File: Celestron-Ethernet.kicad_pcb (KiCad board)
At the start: 4 copper layers, 90.4 x 33.3 mm, 59 parts, among them J2 6P6C, J3 RJ45_Abracon_ARJP11A-MASA-B-A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, U2 LP2985-5.0, U3 LP2985-3.3

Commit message: Initial routing
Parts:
- added REF**: MountingHole_3.2mm_M3, MountingHole:MountingHole_3.2mm_M3, F.Cu at (189.7, 97.5)
- added REF**: MountingHole_3.2mm_M3, MountingHole:MountingHole_3.2mm_M3, F.Cu at (108.2, 97.5)
- added REF**: MountingHole_3.2mm_M3, MountingHole:MountingHole_3.2mm_M3, F.Cu at (108.2, 72.9)
- moved R15 4.57 mm to (133.6, 97.3)
- moved C17 4.57 mm to (124.5, 97.3), turned to 270 degrees
- moved C13 2.29 mm to (131.3, 97.3)
- moved C14 2.29 mm to (129.0, 97.3)
- moved R25 2.29 mm to (119.9, 97.3), turned to 270 degrees
- moved C15 2.29 mm to (122.2, 97.3)
- moved W5500 1.02 mm to (134.1, 85.2)
- moved DHCP 0.92 mm to (187.2, 74.9)
- moved C3 0.92 mm to (160.3, 76.7)
- moved R1 0.92 mm to (162.6, 76.7)
- moved R2 0.92 mm to (164.8, 76.7)
- moved USB 0.77 mm to (162.6, 72.1)
- moved USB PWR 0.76 mm to (170.9, 73.7)
- moved 25Mhz 0.51 mm to (143.0, 85.2)
- moved U2 0.25 mm to (173.0, 97.3)
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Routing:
- net GND: track 0.00 -> 78.3 mm, vias 0 -> 4
- net Net-(C5-Pad1): track 0.00 -> 56.4 mm, vias 0 -> 2
- net Net-(C17-Pad1): track 0.00 -> 29.6 mm
- net Net-(SW1-Pad2): track 0.00 -> 19.8 mm
- net Net-(J2-Pad2): track 0.00 -> 19.1 mm
- net Net-(J2-Pad6): track 0.00 -> 15.4 mm
- net Net-(R16-Pad2): track 0.00 -> 14.4 mm
- net Net-(J1-Pad6): track 0.00 -> 12.6 mm
- net Net-(C18-Pad2): track 0.00 -> 12.3 mm
- net Net-(R12-Pad2): track 0.00 -> 11.6 mm
- net Net-(R18-Pad2): track 0.00 -> 11.2 mm
- net Net-(J3-Pad2): track 0.00 -> 11.1 mm
- net Net-(R14-Pad2): track 0.00 -> 11.0 mm
- net Net-(D3-Pad1): track 0.00 -> 10.8 mm
- net Net-(C7-Pad2): track 0.00 -> 10.3 mm
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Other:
- board size 90.4 x 33.3 mm -> 88.9 x 31.8 mm
- net class Default: clearance 0.2 -> 0.1524; trace_width 0.25 -> 0.1524; via_dia 0.8 -> 0.4572; via_drill 0.4 -> 0.2286
- net class Power added: clearance 0.1524, trace_width 0.4064, via_dia 0.8128, via_drill 0.4064
- rule pad_to_mask_clearance: 0 -> 0.0508
- rule trace_clearance: 0.2 -> 0.1524
- rule trace_min: 0.2 -> 0.1524
- rule via_min_drill: 0.3 -> 0.2286
- rule via_min_size: 0.4 -> 0.4572

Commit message: bypass caps
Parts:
- removed the REF** at (108.2, 72.9)
- added C19: 6.8nF, Capacitor_SMD:C_0603_1608Metric, F.Cu at (114.8, 110.5)
- added C20: 100nF, Capacitor_SMD:C_0603_1608Metric, F.Cu at (126.2, 98.6)
- added C21: 100nF, Capacitor_SMD:C_0603_1608Metric, F.Cu at (126.2, 94.7)
- added C22: 6.8nF, Capacitor_SMD:C_0603_1608Metric, F.Cu at (124.0, 110.5)
- added C23: 22nF, Capacitor_SMD:C_0603_1608Metric, F.Cu at (117.1, 86.6)
- added C24: 100nF, Capacitor_SMD:C_0603_1608Metric, F.Cu at (130.8, 106.2)
- added C25: 100nF, Capacitor_SMD:C_0603_1608Metric, F.Cu at (135.4, 106.2)
- added C26: 100nF, Capacitor_SMD:C_0603_1608Metric, F.Cu at (133.1, 106.2)
- added C27: 1nF/2KV, Capacitor_SMD:C_0603_1608Metric, F.Cu at (112.5, 110.5)
- added FB1: HH-1M1608-121JT, Inductor_SMD:L_0603_1608Metric, F.Cu at (137.7, 106.2)
- added REF**: MountingHole_3.2mm_M3, MountingHole:MountingHole_3.2mm_M3, F.Cu at (186.9, 86.1)
- added REF**: MountingHole_3.2mm_M3, MountingHole:MountingHole_3.2mm_M3, F.Cu at (105.2, 86.1)
- C15: value 10nF -> 10uF
- C16: value 6.8nF -> 100nF
- C17: value 6.8nF -> 10nF
- C18: value 22nF -> 100nF
- JP1: renamed from USB PWR
- R18: value 12K4 -> 12.4K
- moved C18 29.6 mm to (126.2, 102.4)
- moved R22 26.0 mm to (135.4, 110.5)
- moved C16 25.2 mm to (140.0, 102.4)
- moved C15 20.7 mm to (142.2, 102.4), turned to 270 degrees
- moved SW1 16.5 mm to (177.3, 88.1)
- moved C3 16.4 mm to (150.6, 89.9)
- moved R1 16.2 mm to (153.2, 89.9)
- moved R2 16.1 mm to (155.7, 89.9)
- moved J1 15.6 mm to (154.2, 85.3)
- moved JP1 15.6 mm to (162.6, 86.9)
- moved R3 15.5 mm to (150.6, 102.4)
- moved REF** 13.6 mm to (105.2, 110.7)
- moved D3 13.5 mm to (169.7, 98.4)
- moved U1 13.5 mm to (159.9, 98.4)
- moved C1 13.5 mm to (162.1, 112.3)
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- renumbered C8 to C10, C10 to C11, C11 to C5, C9 to C6, C5 to C7, C6 to C8, C7 to C9, PWR to D4, USB to J1, DHCP to SW1, ATmega32U4-AU to U1, W5500 to U4, 16MHz to Y1, 25Mhz to Y2
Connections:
- net Net-(C5-Pad1) renamed /12V
- C15 pad 1: GND -> +3V3
- C15 pad 2: Net-(C15-Pad2) -> GND
- C16 pad 1: Net-(C16-Pad1) -> +3V3
- C16 pad 2: Net-(C16-Pad2) -> GND
- C17 pad 1: Net-(C17-Pad1) -> GND
- C18 pad 1: GND -> +3.3VA
- C18 pad 2: Net-(C18-Pad2) -> GND
- J3 pad 15: Net-(J3-Pad15) -> GNDPWR
- J3 pad 3: Net-(C17-Pad1) -> Net-(C22-Pad1)
- J3 pad 4: Net-(C18-Pad2) -> Net-(C23-Pad2)
- J3 pad 5: Net-(C15-Pad2) -> Net-(C17-Pad2)
- J3 pad 6: Net-(C16-Pad1) -> Net-(C19-Pad1)
- R24 pad 1: Net-(C15-Pad2) -> Net-(C17-Pad2)
- R24 pad 2: Net-(C16-Pad2) -> Net-(C19-Pad2)
- R25 pad 1: Net-(C15-Pad2) -> Net-(C17-Pad2)
- R25 pad 2: Net-(C17-Pad2) -> Net-(C22-Pad2)
- R26 pad 1: Net-(C18-Pad2) -> Net-(C23-Pad2)
- U4 pad 11: +3V3 -> +3.3VA
- U4 pad 15: +3V3 -> +3.3VA
- U4 pad 17: +3V3 -> +3.3VA
- U4 pad 21: +3V3 -> +3.3VA
- U4 pad 4: +3V3 -> +3.3VA
- U4 pad 5: Net-(C16-Pad1) -> Net-(C19-Pad1)
- U4 pad 6: Net-(C17-Pad1) -> Net-(C22-Pad1)
- U4 pad 8: +3V3 -> +3.3VA
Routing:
- net GND: track 78.3 -> 0.00 mm, vias 4 -> 0
- net /12V: track 56.4 -> 0.00 mm, vias 2 -> 0
- net Net-(C17-Pad1): track 29.6 -> 0.00 mm
- net Net-(SW1-Pad2): track 19.8 -> 0.00 mm
- net Net-(J2-Pad2): track 19.1 -> 0.00 mm
- net Net-(J2-Pad6): track 15.4 -> 0.00 mm
- net Net-(R16-Pad2): track 14.4 -> 0.00 mm
- net Net-(J1-Pad6): track 12.6 -> 0.00 mm
- net Net-(C18-Pad2): track 12.3 -> 0.00 mm
- net Net-(R12-Pad2): track 11.6 -> 0.00 mm
- net Net-(R18-Pad2): track 11.2 -> 0.00 mm
- net Net-(J3-Pad2): track 11.1 -> 0.00 mm
- net Net-(R14-Pad2): track 11.0 -> 0.00 mm
- net Net-(D3-Pad1): track 10.8 -> 0.00 mm
- net Net-(C9-Pad2): track 10.3 -> 0.00 mm
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
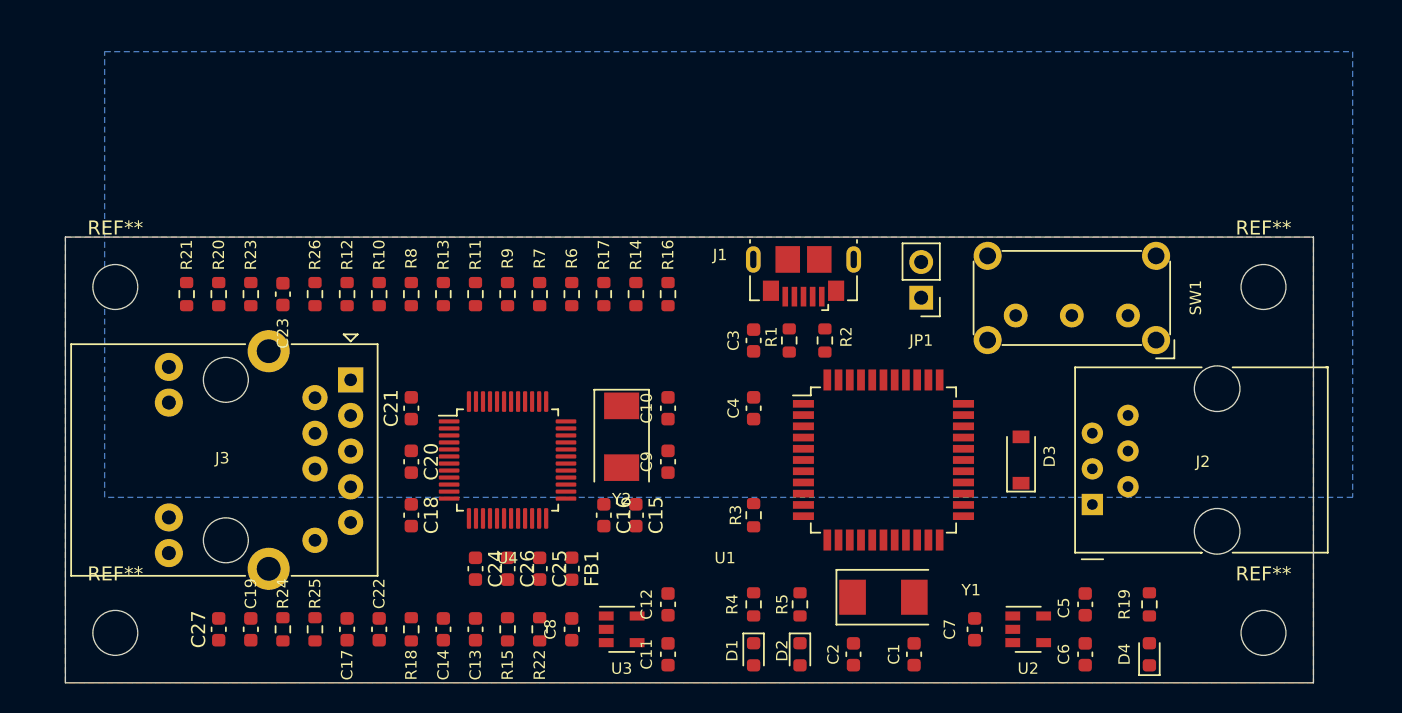
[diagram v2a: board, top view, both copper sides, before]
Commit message: corrected w5500 schematic, added mounting holes
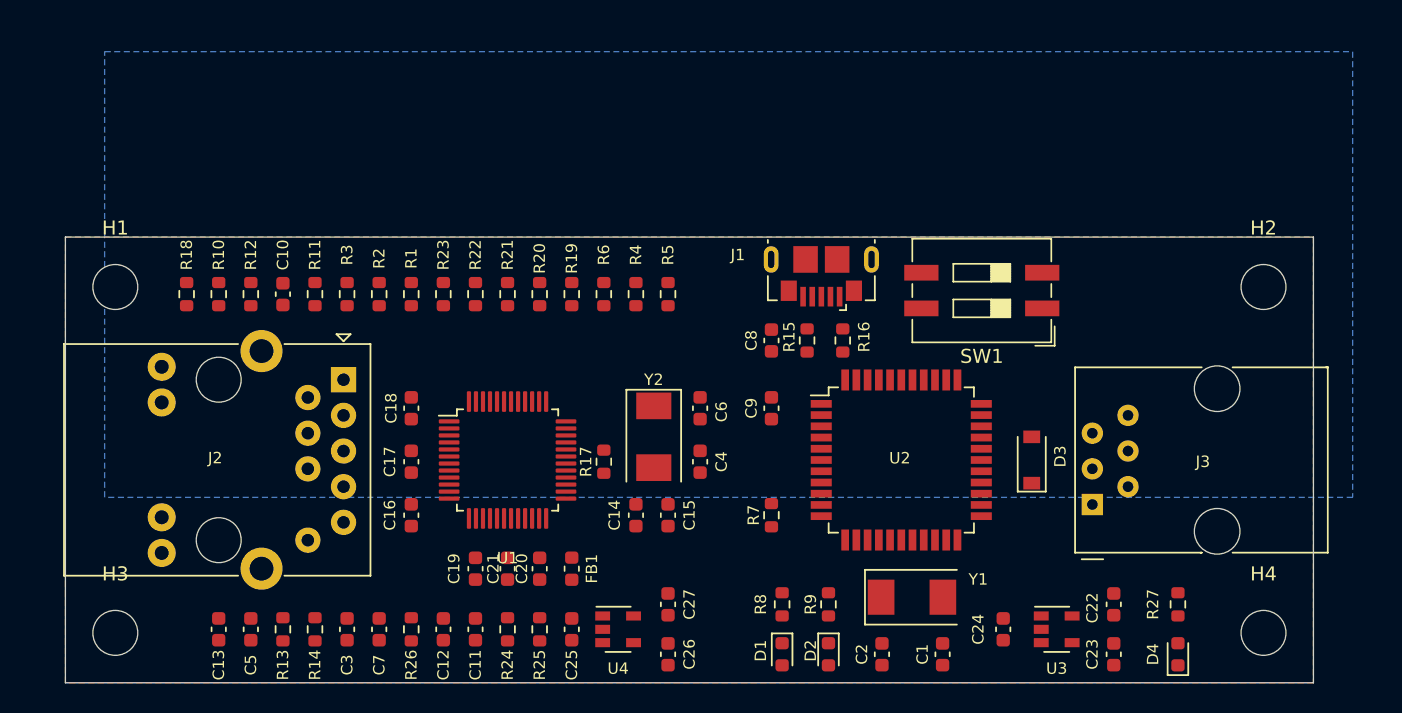
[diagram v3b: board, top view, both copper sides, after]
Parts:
- removed the C3 at (150.6, 89.9)
- removed the C4 at (150.6, 94.7)
- removed JP1: USB PWR, Connector_PinHeader_2.54mm:PinHeader_1x02_P2.54mm_Vertical
- removed the R3 at (150.6, 102.4)
- removed REF** (x4): MountingHole_3.2mm_M3, MountingHole:MountingHole_3.2mm_M3
- removed the U1 at (159.9, 98.4)
- added C8: 100nF, Capacitor_SMD:C_0603_1608Metric, F.Cu at (151.9, 89.9)
- added C9: 100nF, Capacitor_SMD:C_0603_1608Metric, F.Cu at (151.9, 94.7)
- added H1: MountingHole, MountingHole:MountingHole_3.2mm_M3, F.Cu at (105.2, 86.1)
- added H2: MountingHole, MountingHole:MountingHole_3.2mm_M3, F.Cu at (186.9, 86.1)
- added H3: MountingHole, MountingHole:MountingHole_3.2mm_M3, F.Cu at (105.2, 110.7)
- added H4: MountingHole, MountingHole:MountingHole_3.2mm_M3, F.Cu at (186.9, 110.7)
- added R17: 1M, Resistor_SMD:R_0603_1608Metric, F.Cu at (140.0, 98.6)
- added R7: 10K, Resistor_SMD:R_0603_1608Metric, F.Cu at (151.9, 102.4)
- added U2: ATmega32U4-AU, Package_QFP:TQFP-44_10x10mm_P0.8mm, F.Cu at (161.1, 98.4)
- FB1: value HH-1M1608-121JT -> 60 ohm/100MHz
- SW1: value SW_SPDT -> SW_DIP_x02; footprint Button_Switch_THT:SW_E-Switch_EG1224_SPDT_Angled -> Button_Switch_SMD:SW_DIP_SPSTx02_Slide_9.78x7.26mm_W8.61mm_P2.54mm
- moved SW1 10.6 mm to (166.9, 86.4)
- moved C14 2.29 mm to (144.5, 102.4)
- moved C15 2.29 mm to (142.2, 102.4)
- moved C4 2.29 mm to (146.8, 98.6)
- moved C6 2.29 mm to (146.8, 94.7)
- moved Y2 2.29 mm to (143.5, 96.8)
- moved C1 2.03 mm to (164.1, 112.3)
- moved C22 2.03 mm to (176.3, 108.7)
- moved C23 2.03 mm to (176.3, 112.3)
- moved D4 2.03 mm to (180.8, 112.3)
- moved R27 2.03 mm to (180.8, 108.7)
- moved Y1 2.03 mm to (161.9, 108.2)
- moved C2 2.03 mm to (159.8, 112.3)
- moved C24 2.03 mm to (168.4, 110.5)
- moved D1 2.03 mm to (152.7, 112.3)
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- renumbered C23 to C10, C13 to C11, C14 to C12, C27 to C13, C15 to C14, C16 to C15, C18 to C16, C20 to C17, C21 to C18, C24 to C19, C25 to C20, C26 to C21, C5 to C22, C6 to C23, C7 to C24, C8 to C25, C11 to C26, C12 to C27, C17 to C3, C9 to C4, C19 to C5, C10 to C6, C22 to C7, J3 to J2, J2 to J3, R8 to R1, R20 to R10, R26 to R11, R23 to R12, R24 to R13, R25 to R14, R1 to R15, R2 to R16, R21 to R18, R6 to R19, R10 to R2, R7 to R20, R9 to R21, R11 to R22, R13 to R23, R15 to R24, R22 to R25, R18 to R26, R19 to R27, R12 to R3, R14 to R4, R16 to R5, R17 to R6, R4 to R8, R5 to R9, U4 to U1, U2 to U3, U3 to U4
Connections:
- C5 pad 1: Net-(C19-Pad1) -> Net-(C5-Pad1)
- C5 pad 2: Net-(C19-Pad2) -> Net-(C5-Pad2)
- C7 pad 1: Net-(C22-Pad1) -> Net-(C7-Pad1)
- C7 pad 2: Net-(C22-Pad2) -> Net-(C7-Pad2)
- J1 pad 1: Net-(J1-Pad1) -> /USB_PWR
- J2 pad 3: Net-(C22-Pad1) -> Net-(C7-Pad1)
- J2 pad 6: Net-(C19-Pad1) -> Net-(C5-Pad2)
- R13 pad 2: Net-(C19-Pad2) -> Net-(C5-Pad1)
- R14 pad 2: Net-(C22-Pad2) -> Net-(C7-Pad2)
- R4 pad 2: Net-(R14-Pad2) -> Net-(R4-Pad2)
- R5 pad 2: Net-(R16-Pad2) (its old number) -> Net-(R5-Pad2)
- R6 pad 1: Net-(R17-Pad1) -> +3V3
- R6 pad 2: GND -> Net-(R6-Pad2)
- SW1 pad 1: GND -> /USB_PWR
- SW1 pad 2: Net-(SW1-Pad2) -> /DCHP_ENA
- SW1 pad 3: Net-(SW1-Pad3) -> GND
- U1 pad 32: Net-(R16-Pad2) (its old number) -> Net-(R6-Pad2)
- U1 pad 36: Net-(R14-Pad2) -> Net-(R5-Pad2)
- U1 pad 37: Net-(R17-Pad1) -> Net-(R4-Pad2)
- U1 pad 5: Net-(C19-Pad1) -> Net-(C5-Pad1)
- U1 pad 6: Net-(C22-Pad1) -> Net-(C7-Pad2)

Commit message: traces complete
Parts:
- removed the C15 at (142.2, 102.4)
- removed the C25 at (137.7, 110.5)
- removed the C4 at (146.8, 98.6)
- removed the C9 at (151.9, 94.7)
- removed D4: Red, LED_SMD:LED_0603_1608Metric
- removed the R14 at (119.4, 110.5)
- removed the R15 at (154.4, 89.9)
- removed R25: 330R, Resistor_SMD:R_0603_1608Metric
- removed R26: 12.4K, Resistor_SMD:R_0603_1608Metric
- removed R27: 1K, Resistor_SMD:R_0603_1608Metric
- removed the R8 at (152.7, 108.7)
- removed the R9 at (156.0, 108.7)
- removed the U4 at (141.0, 110.5)
- added C1: 100nF, Capacitor_SMD:C_0603_1608Metric, F.Cu at (171.4, 94.5)
- added C10: 100nF, Capacitor_SMD:C_0603_1608Metric, F.Cu at (167.4, 90.7)
- added C20: 100nF, Capacitor_SMD:C_0603_1608Metric, F.Cu at (138.9, 102.4)
- added C22: 100nF, Capacitor_SMD:C_0603_1608Metric, F.Cu at (171.4, 98.6)
- added C23: 100nF, Capacitor_SMD:C_0603_1608Metric, F.Cu at (157.2, 94.5)
- added C27: 1uF, Capacitor_SMD:C_0603_1608Metric, F.Cu at (141.0, 110.2)
- added C28: 1uF, Capacitor_SMD:C_0603_1608Metric, F.Cu at (153.2, 110.2)
- added R10: 330R, Resistor_SMD:R_0603_1608Metric, F.Cu at (171.4, 102.4)
- added R11: 82R, Resistor_SMD:R_0603_1608Metric, F.Cu at (124.7, 110.2)
- added R12: 82R, Resistor_SMD:R_0603_1608Metric, F.Cu at (126.7, 110.2)
- added R23: 12.4K, Resistor_SMD:R_0603_1608Metric, F.Cu at (132.8, 110.2)
- added SW2: DHCP, Button_Switch_THT:SW_E-Switch_EG1224_SPDT_Angled, F.Cu at (168.9, 108.7)
- added U3: LP2985-3.3, Package_TO_SOT_SMD:SOT-23-5, F.Cu at (144.0, 110.2)
- C11: value 10nF -> 1nF/2KV; footprint Capacitor_SMD:C_0603_1608Metric -> Capacitor_SMD:C_1206_3216Metric
- C13: value 1nF/2KV -> 10nF
- C2: renamed from C1; value 22pF -> 18pF
- C24: value 1uF -> 10uF
- C3: value 10nF -> 6.8nF
- C4: renamed from C2; value 22pF -> 18pF
- C7: value 6.8nF -> 18pF
- C8: value 100nF -> 10nF
- D1: value Ylw -> Red
- D2: value Grn -> 1N4148W; footprint LED_SMD:LED_0603_1608Metric -> Diode_SMD:D_SOD-323F
- D3: value 1N4148W -> Red; footprint Diode_SMD:D_SOD-123 -> LED_SMD:LED_0603_1608Metric
- J1: value USB_B_Micro -> FTDI; footprint Connector_USB:USB_Micro-B_GCT_USB3076-30-A -> Connector_PinHeader_2.54mm:PinHeader_1x06_P2.54mm_Horizontal
- J2: value RJ45_Abracon_ARJP11A-MASA-B-A-EMU2 -> RJ45_Amphenol_RJMG1BD3B8K1ANR; footprint Connector_RJ:RJ45_Abracon_ARJP11A-MA_Horizontal -> Connector_RJ:RJ45_Amphenol_RJMG1BD3B8K1ANR
- R13: value 49R9 -> 1M
- R16: value 22R -> 330R
- R17: value 1M -> 10K
- R24: value 10K -> 1K
- SW1: value SW_DIP_x02 -> SW_Push; footprint Button_Switch_SMD:SW_DIP_SPSTx02_Slide_9.78x7.26mm_W8.61mm_P2.54mm -> Button_Switch_SMD:SW_SPST_FSMSM
- U2: value ATmega32U4-AU -> ATmega328-AU; footprint Package_QFP:TQFP-44_10x10mm_P0.8mm -> Package_QFP:TQFP-32_7x7mm_P0.8mm
- moved R16 41.6 mm to (120.7, 110.2)
- moved C8 30.8 mm to (128.8, 110.2)
- moved R24 30.5 mm to (163.3, 106.2)
- moved R13 24.9 mm to (138.9, 98.6)
- moved C13 24.4 mm to (136.9, 110.2)
- moved C7 24.2 mm to (145.0, 98.6)
- moved D1 23.1 mm to (173.5, 102.4)
- moved C24 22.1 mm to (153.2, 94.5), turned to 90 degrees
- moved D2 21.7 mm to (159.3, 90.8), turned to 90 degrees
- moved R14 17.8 mm to (165.4, 90.7)
- moved C2 17.5 mm to (153.2, 98.6), turned to 270 degrees
- moved C30 17.2 mm to (159.3, 106.2)
- moved C29 17.1 mm to (159.3, 110.2), turned to 90 degrees
- moved C5 16.0 mm to (130.8, 110.2)
- moved U4 16.0 mm to (156.2, 110.2)
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- renumbered C21 to C14, C20 to C15, C19 to C16, C18 to C17, C17 to C18, C16 to C19, C14 to C21, C27 to C25, C23 to C29, C22 to C30, C10 to C9, R6 to R1, R7 to R14, R18 to R15, R23 to R18, R22 to R19, R5 to R2, R21 to R20, R20 to R21, R19 to R22, R4 to R3, R3 to R4, R2 to R5, R1 to R6, R12 to R7, R11 to R8, R10 to R9, U3 to U4
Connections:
- C11 pad 2: Net-(C11-Pad2) -> GNDPWR
- C13 pad 2: GNDPWR -> Net-(C13-Pad2)
- C2 pad 2: Net-(C1-Pad2) -> Net-(C2-Pad2)
- C24 pad 1: /12V -> +5V
- C3 pad 1: GND -> Net-(C3-Pad1)
- C3 pad 2: Net-(C3-Pad2) -> /RD+
- C4 pad 2: Net-(C2-Pad2) -> Net-(C4-Pad2)
- C5 pad 1: Net-(C5-Pad1) -> /RD-
- C7 pad 1: Net-(C7-Pad1) -> GND
- C8 pad 1: Net-(C8-Pad1) -> GND
- C8 pad 2: GND -> /RCT
- C9 pad 2: Net-(C10-Pad2) -> /TCT
- D1 pad 1: Net-(D1-Pad1) -> GND
- D1 pad 2: +5V -> Net-(D1-Pad2)
- D2 pad 2: +5V -> /TXO
- D3 pad 1: Net-(D3-Pad1) -> GND
- J1 pad 1: /USB_PWR -> GND
- J1 pad 2: Net-(J1-Pad2) -> GND
- J1 pad 3: Net-(J1-Pad3) -> +5V
- J1 pad 4: Net-(J1-Pad4) -> /RXI
- J1 pad 5: GND -> /TXO
- J1 pad 6: Net-(J1-Pad6) -> /DTR
- J2 pad 13: +3V3 -> GNDPWR
- J3 pad 2: Net-(J3-Pad2) -> /RXI
- J3 pad 3: /12V -> +12V
- J3 pad 4: Net-(D3-Pad2) -> /TXO
- J3 pad 6: Net-(J3-Pad6) -> /D8
- R13 pad 1: Net-(C3-Pad2) -> Net-(C7-Pad2)
- R13 pad 2: Net-(C5-Pad1) -> Net-(C6-Pad2)
- R14 pad 2: Net-(R7-Pad2) -> Net-(C10-Pad1)
- R15 pad 1: Net-(J2-Pad12) -> /LEDG_K
- R16 pad 1: Net-(J1-Pad2) -> /LEDY_K
- R17 pad 1: Net-(C6-Pad2) -> Net-(R17-Pad1)
- R17 pad 2: Net-(C4-Pad2) -> GND
- R24 pad 1: Net-(R24-Pad1) -> +5V
- R24 pad 2: GND -> Net-(D3-Pad2)
- R7 pad 1: Net-(J2-Pad1) -> /TD-
- R7 pad 2: +3V3 -> +3.3VA
- R8 pad 1: Net-(C10-Pad2) -> /TCT
- R8 pad 2: +3V3 -> +3.3VA
- R9 pad 1: Net-(J2-Pad2) -> /TD+
- R9 pad 2: +3V3 -> +3.3VA
- SW1 pad 1: /USB_PWR -> GND
- SW1 pad 2: /DCHP_ENA -> Net-(C10-Pad1)
- U1 pad 1: Net-(J2-Pad2) -> /TD-
- U1 pad 2: Net-(J2-Pad1) -> /TD+
- U1 pad 22: Net-(C11-Pad2) -> Net-(C13-Pad2)
- U1 pad 23: Net-(R24-Pad1) -> Net-(R17-Pad1)
- U1 pad 27: Net-(R25-Pad2) -> Net-(R16-Pad2)
- U1 pad 30: Net-(C4-Pad2) -> Net-(C6-Pad2)
- U1 pad 31: Net-(C6-Pad2) -> Net-(C7-Pad2)
- U1 pad 33: Net-(U1-Pad33) -> /SCK
- U1 pad 34: Net-(U1-Pad34) -> /MISO
- U1 pad 35: Net-(U1-Pad35) -> /MOSI
- U1 pad 5: Net-(C5-Pad1) -> Net-(C5-Pad2)
- U1 pad 6: Net-(C7-Pad2) -> Net-(C3-Pad1)
- U2 pad 10: Net-(U1-Pad34) -> Net-(U2-Pad10)
- U2 pad 11: Net-(U1-Pad35) -> Net-(U2-Pad11)
- U2 pad 13: Net-(R7-Pad2) -> Net-(U2-Pad13)
- U2 pad 14: +5V -> Net-(U2-Pad14)
- U2 pad 15: GND -> /MOSI
- U2 pad 16: Net-(C2-Pad2) -> /MISO
- U2 pad 17: Net-(C1-Pad2) -> /SCK
- U2 pad 18: Net-(U2-Pad18) -> +5V
- U2 pad 2: +5V -> /D8
- U2 pad 20: Net-(J3-Pad2) -> Net-(C1-Pad2)
- U2 pad 21: Net-(D3-Pad1) -> GND
- U2 pad 23: GND -> Net-(U2-Pad23)
- U2 pad 24: +5V -> Net-(U2-Pad24)
- U2 pad 25: Net-(J3-Pad6) -> Net-(U2-Pad25)
- U2 pad 28: /DCHP_ENA -> Net-(U2-Pad28)
- U2 pad 29: Net-(U2-Pad29) -> Net-(C10-Pad1)
- U2 pad 3: Net-(R16-Pad2) -> GND
- U2 pad 30: Net-(U2-Pad30) -> /RXI
- U2 pad 31: Net-(U2-Pad31) -> Net-(D2-Pad1)
- U2 pad 4: Net-(R15-Pad1) -> +5V
- U2 pad 6: Net-(C9-Pad1) -> +5V
- U2 pad 7: +5V -> Net-(C2-Pad2)
- U2 pad 8: Net-(R8-Pad1) -> Net-(C4-Pad2)
- U2 pad 9: Net-(U1-Pad33) -> Net-(U2-Pad9)
- U4 pad 1: /12V -> +12V
- U4 pad 3: /12V -> +12V
- Y1 pad 2: Net-(C1-Pad2) -> Net-(C4-Pad2)
- Y2 pad 1: Net-(C6-Pad2) -> Net-(C7-Pad2)
- Y2 pad 2: Net-(C4-Pad2) -> Net-(C6-Pad2)
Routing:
- net +3V3: track 0.00 -> 93.5 mm, vias 0 -> 12
- net +12V: track 0.00 -> 52.7 mm, vias 0 -> 2
- net GND: track 0.00 -> 45.4 mm, vias 0 -> 20
- net /SCK: track 0.00 -> 39.9 mm, vias 0 -> 2
- net /MISO: track 0.00 -> 39.2 mm, vias 0 -> 2
- net /MOSI: track 0.00 -> 33.6 mm, vias 0 -> 2
- net /RXI: track 0.00 -> 33.2 mm
- net /TXO: track 0.00 -> 32.9 mm
- net +3.3VA: track 0.00 -> 29.0 mm, vias 0 -> 10
- net Net-(R16-Pad2): track 0.00 -> 28.8 mm, vias 0 -> 2
- net Net-(R15-Pad2): track 0.00 -> 26.9 mm, vias 0 -> 2
- net /TD+: track 0.00 -> 23.2 mm, vias 0 -> 1
- net Net-(C5-Pad2): track 0.00 -> 22.4 mm, vias 0 -> 2
- net +5V: track 0.00 -> 22.1 mm, vias 0 -> 6
- net GNDPWR: track 0.00 -> 20.5 mm
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- added copper zone on In2.Cu, net +3.3VA

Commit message: silkscreen
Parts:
- added G***: LOGO, Celestron-Ethernet:asian_tiger, F.Cu at (146.2, 93.7)
- D3: value Red -> Blu
- moved FB1 0.25 mm to (136.1, 91.2)
- moved H4 0.25 mm to (186.9, 111.5)
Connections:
- net Net-(C10-Pad1) renamed /~RST
- net Net-(C3-Pad1) renamed /RXP
- net Net-(C5-Pad2) renamed /RXN
- net Net-(R15-Pad2) renamed /LINKLED
- net Net-(R16-Pad2) renamed /ACTLED
- D2 pad 1: Net-(D2-Pad1) -> /TX
- J1 pad 5: /TXO -> /TX
- U2 pad 31: Net-(D2-Pad1) -> /TX
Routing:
- net GND: track 45.4 -> 65.5 mm, vias 20 -> 71
- net /TX: track 0.00 -> 17.4 mm
- net Net-(D2-Pad1): track 4.42 -> 0.00 mm
- net /TXO: track 32.9 -> 36.7 mm
- net +3V3: track 93.5 -> 96.2 mm, vias 12 -> 13
- net /MISO: track 39.2 -> 40.6 mm
- net /LEDY_K: track 18.5 -> 19.8 mm
- net Net-(R23-Pad2): track 12.8 -> 13.8 mm
- net /ACTLED: track 28.8 -> 29.7 mm
- net /TD+: track 23.2 -> 24.1 mm
- net /LEDG_K: track 14.4 -> 15.2 mm
- net Net-(R20-Pad1): track 9.31 -> 8.76 mm
- net +3.3VA: track 29.0 -> 29.5 mm, vias 10 -> 11
- net Net-(R18-Pad1): track 7.46 -> 6.93 mm
- net Net-(R19-Pad1): track 8.25 -> 7.73 mm
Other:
- board text added: "16Mhz"
- board text added: "25Mhz"
- board text added: "ATmega328-AU"
- board text added: "Celestron Ethernet Adapter v 1.0 by Hyiger Designs"
- board text added: "Client"
- board text added: "DCHP Server"
- board text added: "GND"
- board text added: "On - DCHP Client Off - DHCP Server"
- board text added: "RESET"
- board text added: "RX"
- board text added: "TX"
- board text added: "VCC"
- board text added: "W5500"
- board text added: "https://github.com/Hyiger-Designs/Celestron-Ethernet"
- board text added: "~RTS"
